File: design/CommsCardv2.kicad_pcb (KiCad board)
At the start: 4 copper layers, 100 x 100 mm, 191 parts, among them J1001 USB_B, J201 Conn_01x02, J301 DB9_Male_MountingHoles, J302 DB9_Male_MountingHoles, J303 DB9_Male_MountingHoles, J304 Conn_01x02, J305 Conn_Coaxial, J501 Conn_01x03, J701 Conn_01x03, J901 USB_B, Q301 Q_NMOS_DGS, Q302 Q_NMOS_DGS, U1001 ADUM3160, U201 LT3509EMSE, U301 MAX3387EEUG, U302 MAX3485, U303 TPS28225DRBT, U401 74LV14, U402 74LVC2G00, U403 STWD100xxWY, U404 STWD100xxWY, U405 74AHC157, U501 93C46B, U502 FT4232H, U503 74LV595, U601 74LVC3G14, U602 SN74LV86, U603 501BMILF, U604 74LVC1G80, U605 74LV595, U606 74LV595, U701 93C46B, U702 FT4232H, U703 74LV595, U801 74LVC3G14, U802 SN74LV86, U803 501BMILF, U804 74LVC1G80, U805 74LV595, U806 74LV595, U901 ADUM3160, X501 ASEMB-12MHz, X701 ASEMB-12MHz

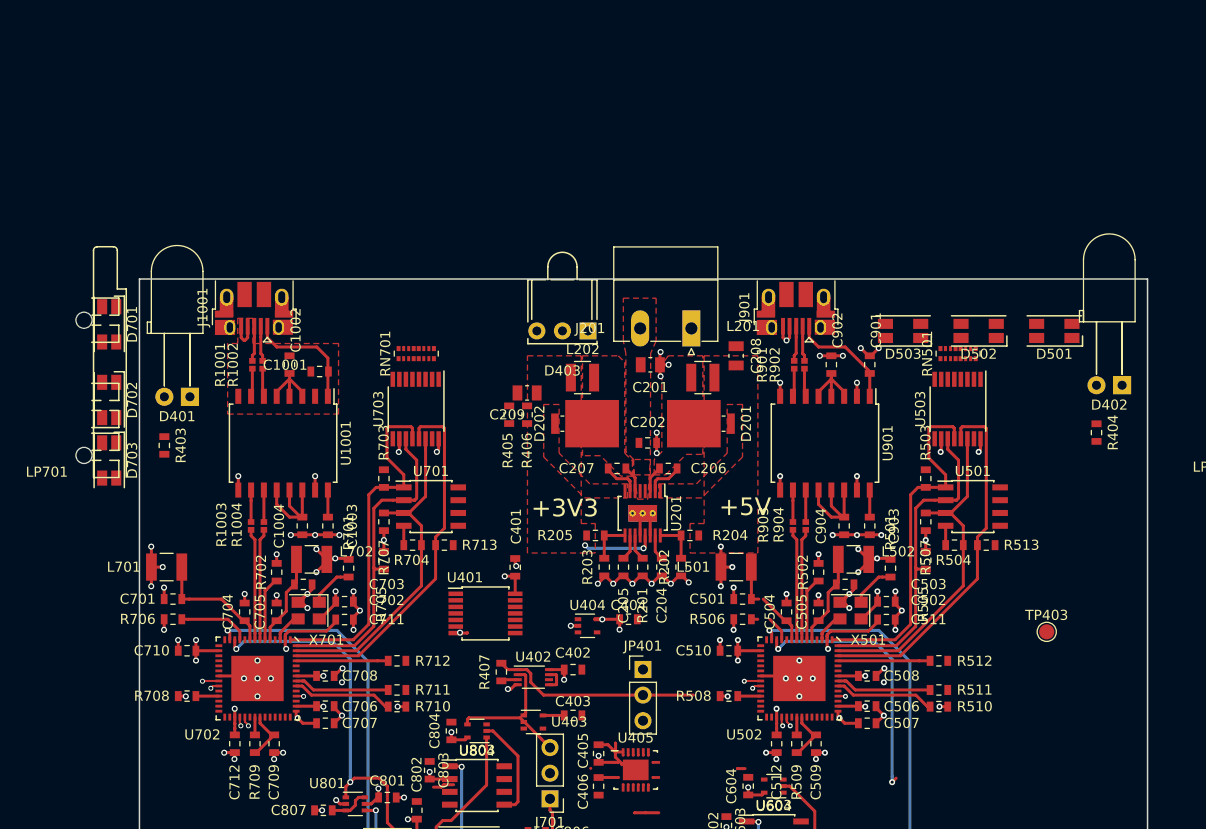
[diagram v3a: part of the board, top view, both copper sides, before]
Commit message: Adding smaller light pipe and compressing power input
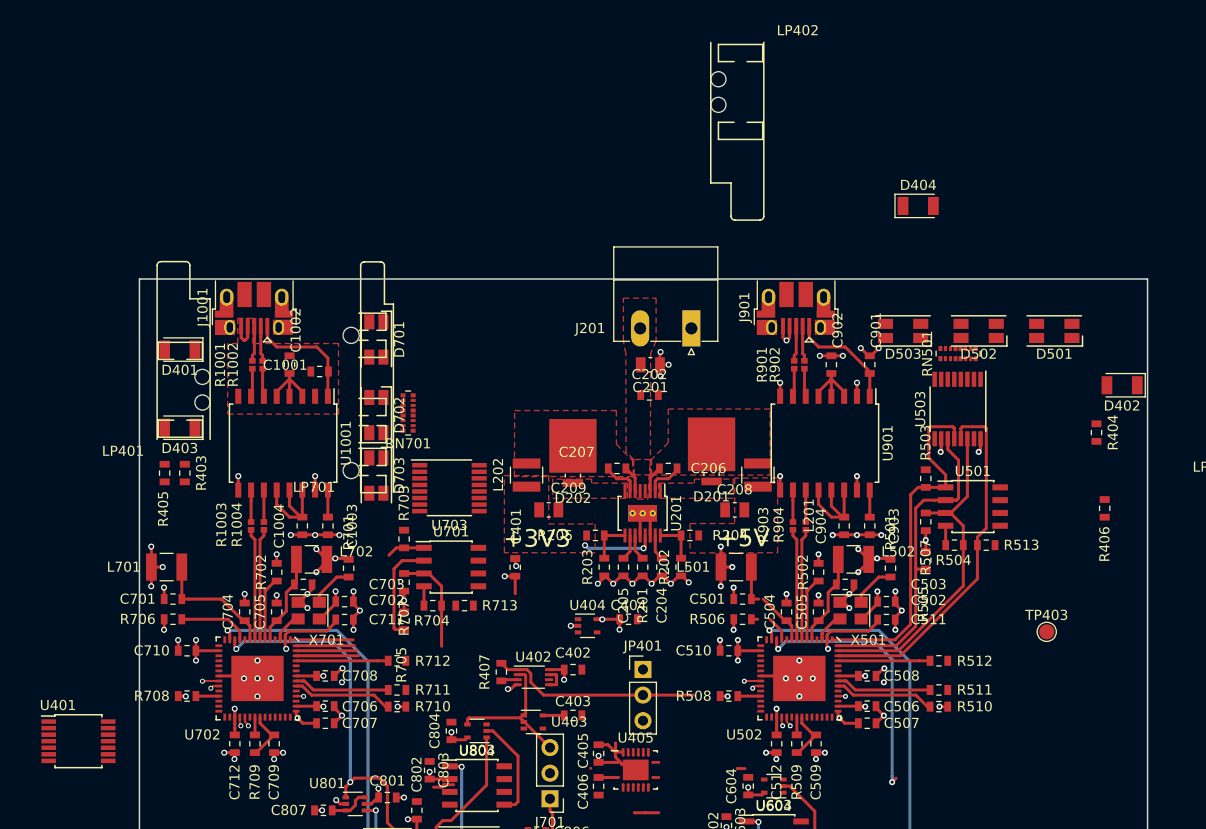
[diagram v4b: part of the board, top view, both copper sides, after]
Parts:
- added D404: Blue, LED_SMD:LED_1206_3216Metric, F.Cu at (112.2, 30.8)
- added LP401: LightPipe, LEDs:Lumex_LPF-C012303S, F.Cu at (41.2, 50.2)
- added LP402: LightPipe, LEDs:Lumex_LPF-C012303S, F.Cu at (92.4, 18.2)
- D401, D402: footprint LED_THT:LED_D5.0mm_Horizontal_O6.35mm_Z9.0mm -> LED_SMD:LED_1206_3216Metric
- D403: value LED_Dual_ACA -> Blue; footprint LEDs:WP130WDT -> LED_SMD:LED_1206_3216Metric
- moved R406 58.0 mm to (130.8, 60.8)
- moved U401 42.3 mm to (28.9, 83.8)
- moved D403 41.6 mm to (39.0, 52.8)
- moved R405 34.7 mm to (37.5, 57.2)
- moved D701 26.5 mm to (58.5, 44.0)
- moved D702 26.5 mm to (58.5, 51.5)
- moved D703 26.5 mm to (58.5, 57.5)
- moved LP701 26.5 mm to (56.0, 57.0)
- moved C208 15.3 mm to (94.0, 60.9), turned to 180 degrees
- moved C209 11.8 mm to (75.6, 60.9), turned to 0 degrees
- moved L202 11.1 mm to (73.4, 57.5), turned to 90 degrees
- moved L201 11.1 mm to (96.3, 57.5), turned to 90 degrees
- moved U703 8.53 mm to (65.8, 58.8), turned to 0 degrees
- moved R703 6.32 mm to (61.2, 63.8)
- moved R704 6.32 mm to (64.1, 70.4)
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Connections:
- D403 pad 1: Net-(D403-Pad1) -> GND
- D403 pad 2: GND -> Net-(D403-Pad2)
- R405 pad 2: Net-(D403-Pad1) -> Net-(D403-Pad2)
- R406 pad 2: Net-(D403-Pad3) -> Net-(D404-Pad2)
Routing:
- net /Watchdog/~FC2_PWREN: track 36.0 -> 6.20 mm
- net /FlightComputer2/EECS: track 35.3 -> 10.0 mm
- net /FlightComputer2/EEDATA: track 33.9 -> 16.2 mm
- net /FlightComputer2/EECLK: track 32.3 -> 16.0 mm
- net GND: track 118.5 -> 115.3 mm, vias 79 -> 76
- net +3V3: track 127.5 -> 124.8 mm, vias 56 -> 54

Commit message: Additional work on power input
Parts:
- C201: moved to B.Cu
- moved J305 121.7 mm to (126.8, 46.5), turned to 270 degrees
- moved D404 36.6 mm to (122.0, 66.0)
- moved LP501 34.8 mm to (110.5, 57.0)
- moved R504 32.4 mm to (141.3, 84.4)
- moved U503 32.4 mm to (141.7, 70.9)
- moved R503 32.4 mm to (138.5, 77.8)
- moved R505 32.4 mm to (138.5, 85.9)
- moved R507 32.4 mm to (138.5, 82.1)
- moved R513 32.4 mm to (144.5, 84.4)
- moved U501 32.4 mm to (143.2, 80.6)
- moved LP402 32.2 mm to (95.5, 50.2), turned to 180 degrees
- moved C401 14.5 mm to (86.7, 66.1)
- moved D202 14.0 mm to (68.8, 44.6)
- moved D503 13.8 mm to (113.2, 56.8), turned to 270 degrees
- moved D501 12.5 mm to (113.2, 44.0), turned to 270 degrees
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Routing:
- net /FlightComputer1/EECS: track 35.3 -> 12.2 mm
- net /Watchdog/~FC1_PWREN: track 36.0 -> 15.7 mm
- net /FlightComputer1/EEDATA: track 33.9 -> 14.7 mm
- net GND: track 115.3 -> 99.7 mm, vias 76 -> 67
- net /FlightComputer1/EECLK: track 32.3 -> 18.0 mm
- net /Watchdog/~FC2_PWREN: track 6.20 -> 17.3 mm
- net /FlightComputer2/EECS: track 10.0 -> 17.4 mm
- net +3V3: track 124.8 -> 117.8 mm, vias 54 -> 51
- net /FlightComputer2/EEDATA: track 16.2 -> 22.1 mm
- net /Power/PWR_IN: vias 0 -> 4
- added copper zone on B.Cu, net /Power/PWR_IN
